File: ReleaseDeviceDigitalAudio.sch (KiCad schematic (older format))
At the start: 7 parts, among them J1 Conn_02x08_Counter_Clockwise

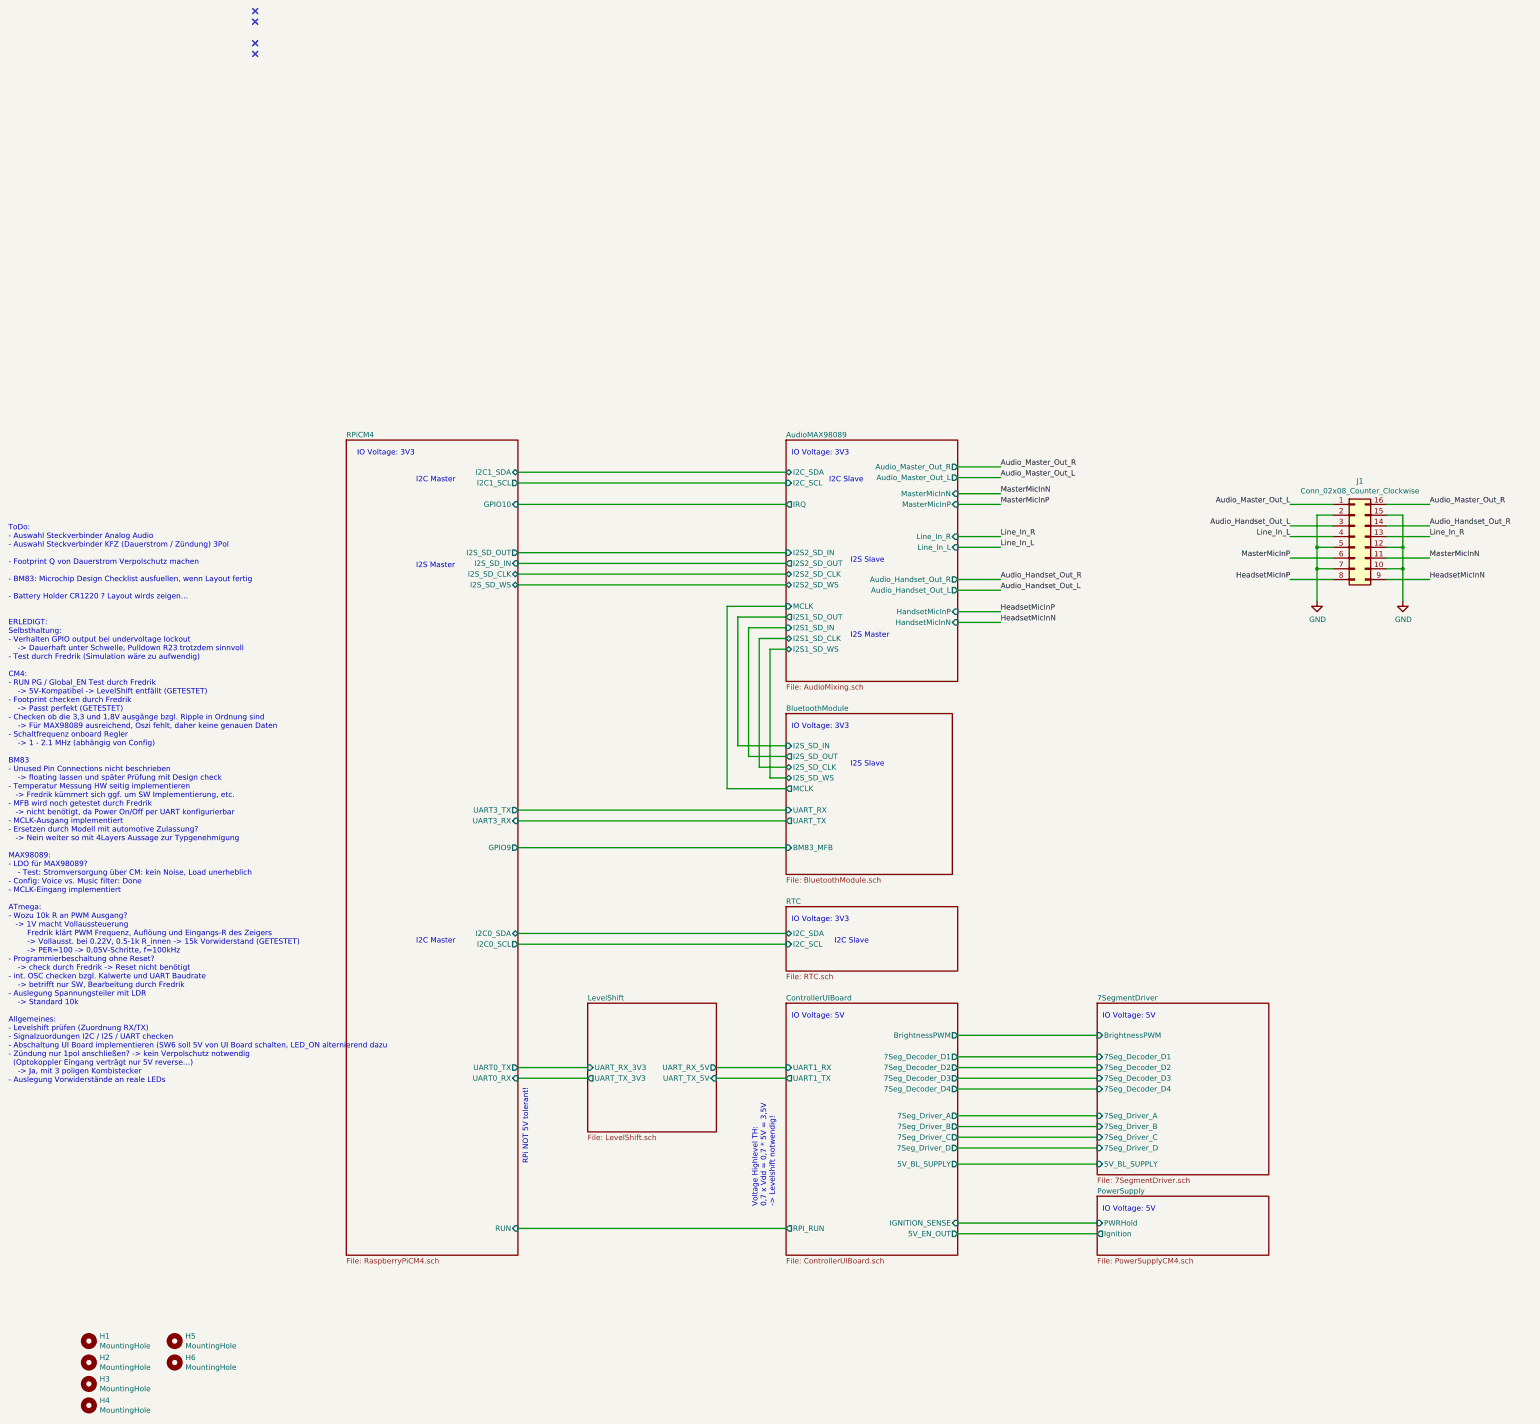
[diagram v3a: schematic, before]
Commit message: - Footprints inkl. 3D model aller Steckverbinder fertig
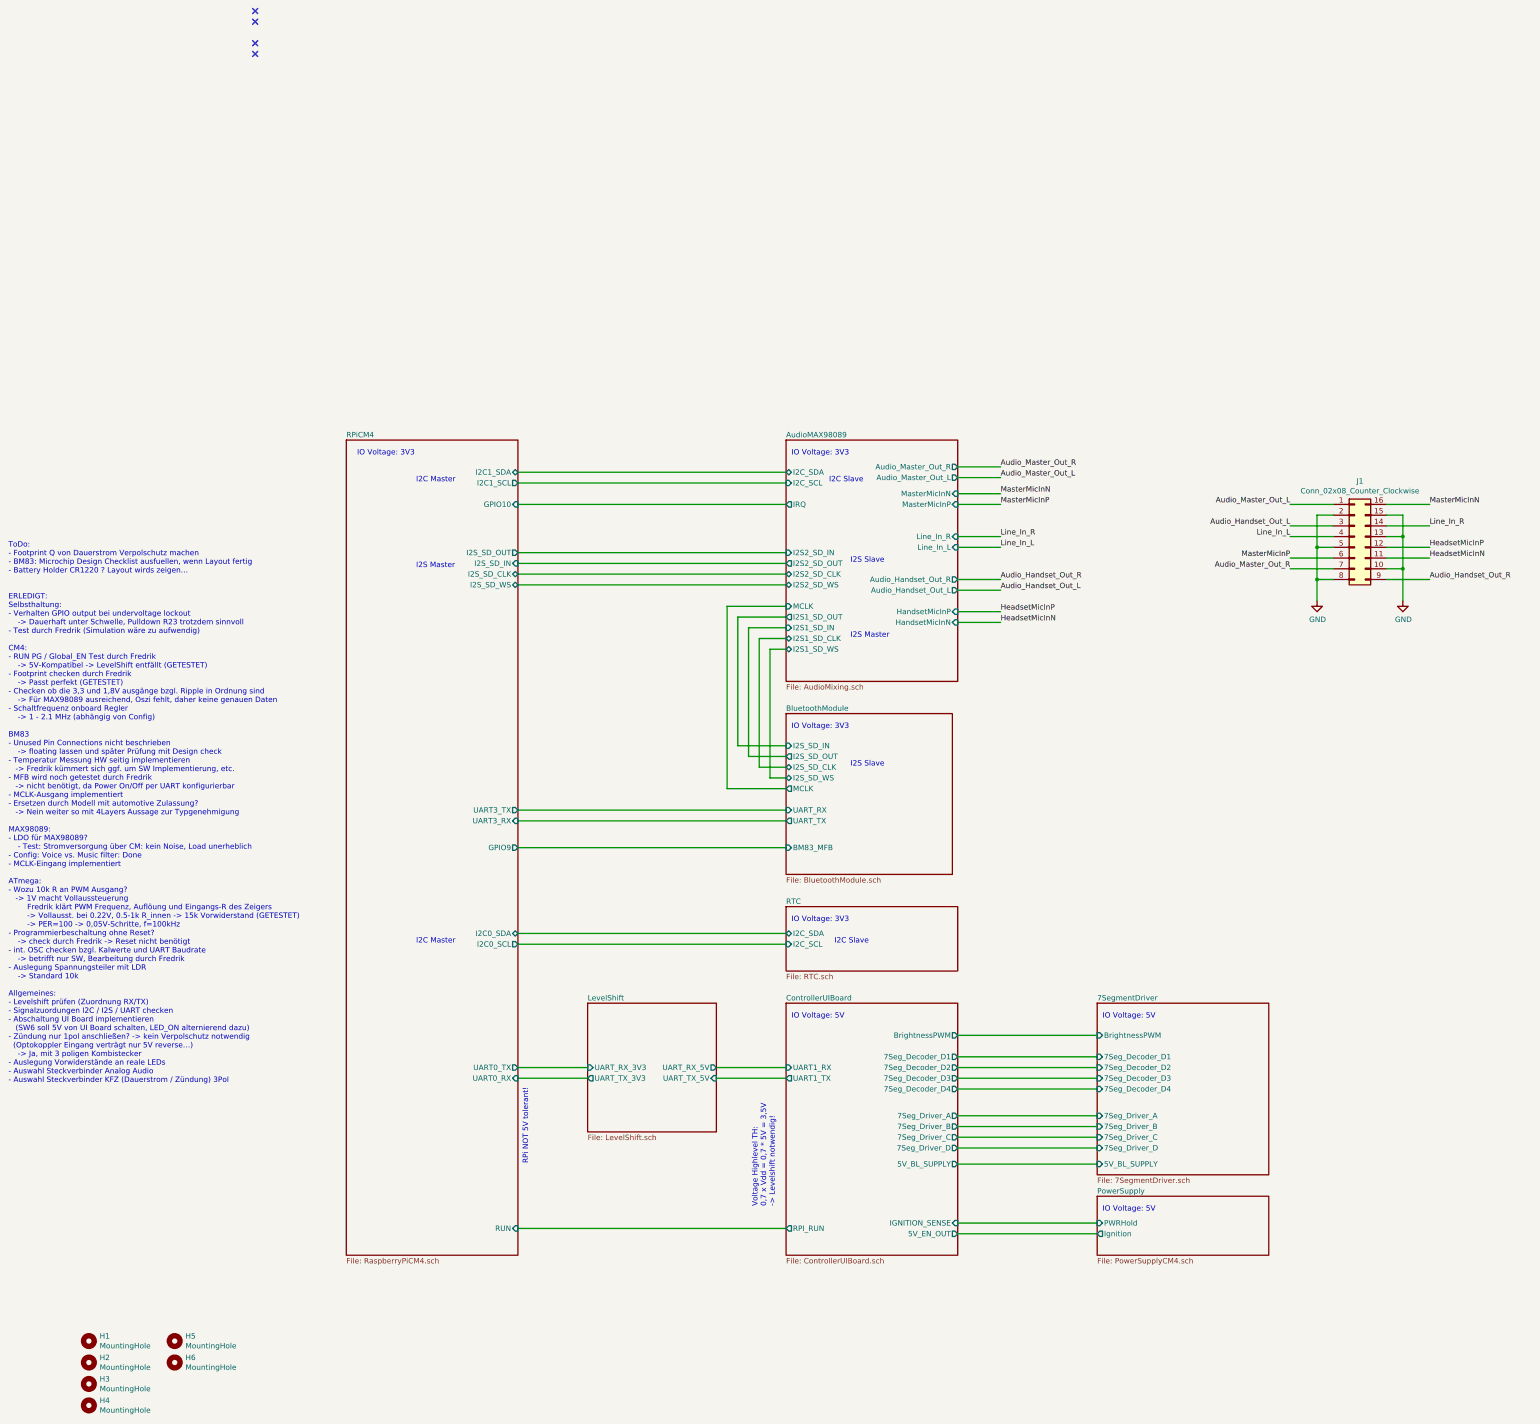
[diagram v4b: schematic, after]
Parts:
- J1: footprint Connector_PinSocket_2.00mm:PinSocket_2x07_P2.00mm_Vertical -> TeKaDe:Molex_34825-0160
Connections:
- net Audio_Handset_Out_R: now also J1.9 (Pin_9); no longer J1.14 (Pin_14)
- net Audio_Master_Out_R: now also J1.7 (Pin_7); no longer J1.16 (Pin_16)
- net GND: now also J1.13 (Pin_13), J1.8 (Pin_8); no longer J1.12 (Pin_12), J1.7 (Pin_7)
- net HeadsetMicInN: now also J1.11 (Pin_11); no longer J1.9 (Pin_9)
- net HeadsetMicInP: now also J1.12 (Pin_12); no longer J1.8 (Pin_8)
- net Line_In_R: now also J1.14 (Pin_14); no longer J1.13 (Pin_13)
- net MasterMicInN: now also J1.16 (Pin_16); no longer J1.11 (Pin_11)
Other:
- note added: "ToDo: \n- Footprint Q von Dauerstrom Verpolschutz machen\n- BM83: Microchip Design Checklist ausfuellen, wenn Layout fertig\n- Battery Holder CR1220 ? Layout wirds zeigen…\n\n\nERLEDIGT:\nSelbsthaltung:\n- Verhalten GPIO output bei undervoltage lockout \n -> Dauerhaft unter Schwelle, Pulldown R23 trotzdem sinnvoll\n- Test durch Fredrik (Simulation wäre zu aufwendig)\n\nCM4: \n- RUN PG / Global_EN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"
- note removed: "ToDo: \n- Auswahl Steckverbinder Analog Audio\n- Auswahl Steckverbinder KFZ (Dauerstrom / Zündung) 3Pol\n\n- Footprint Q von Dauerstrom Verpolschutz machen\n\n- BM83: Microchip Design Checklist ausfuellen, wenn Layout fertig\n\n- Battery Holder CR1220 ? Layout wirds zeigen…\n\n\nERLEDIGT:\nSelbsthaltung:\n- Verhalten GPIO output bei undervoltage lockout \n -> Dauerhaft unter Schwelle, Pulldown R2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"
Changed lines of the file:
@@
 $EndComp
 Text Notes 800  7100 0    50   ~ 0
-ToDo: \n- Auswahl Steckverbinder Analog Audio\n- Auswahl Steckverbinder KFZ (Dauerstrom / Zündung) 3Pol\n\n- Footprint Q von Dauerstrom Verpolschutz machen\n\n- BM83: Microchip Design Checklist ausfuellen, wenn Layout fertig\n\n- Battery Holder CR1220 ? Layout wirds zeigen…\n\n\nERLEDIGT:\nSelbsthaltung:\n- Verhalten GPIO output bei undervoltage lockout \n    -> Dauerhaft unter Schwelle, Pulldown R23 trotzdem sinnvoll\n- Test durch Fredrik (Simulation wäre zu aufwendig)\n\nCM4: \n- RUN PG / Global_EN Test durch Fredrik\n    -> 5V-Kompatibel -> LevelShift entfällt (GETESTET)\n- Footprint checken durch Fredrik\n    -> Passt perfekt (GETESTET)\n- Checken ob die 3,3 und 1,8V ausgänge bzgl. Ripple in Ordnung sind\n    -> Für MAX98089 ausreichend, Oszi fehlt, daher keine genauen Daten\n- Schaltfrequenz onboard Regler\n    -> 1 - 2.1 MHz (abhängig von Config)\n\nBM83\n- Unused Pin Connections nicht beschrieben \n    -> floating lassen und später Prüfung mit Design check\n- Temperatur Messung HW seitig implementieren\n   -> Fredrik kümmert sich ggf. um SW Implementierung, etc.\n- MFB wird noch getestet durch Fredrik  \n   -> nicht benötigt, da Power On/Off per UART konfigurierbar\n- MCLK-Ausgang implementiert\n- Ersetzen durch Modell mit automotive Zulassung?\n   -> Nein weiter so mit 4Layers Aussage zur Typgenehmigung\n\nMAX98089:\n- LDO für MAX98089? \n    - Test: Stromversorgung über CM: kein Noise, Load unerheblich\n- Config: Voice vs. Music filter: Done\n- MCLK-Eingang implementiert\n\nATmega:\n- Wozu 10k R an PWM Ausgang?\n   -> 1V macht Vollaussteuerung\n        Fredrik klärt PWM Frequenz, Auflöung und Eingangs-R des Zeigers\n        -> Vollausst. bei 0.22V, 0.5-1k R_innen -> 15k Vorwiderstand (GETESTET)\n        -> PER=100 -> 0,05V-Schritte, f=100kHz\n- Programmierbeschaltung ohne Reset?\n    -> check durch Fredrik -> Reset nicht benötigt\n- int. OSC checken bzgl. Kalwerte und UART Baudrate\n    -> betrifft nur SW, Bearbeitung durch Fredrik\n- Auslegung Spannungsteiler mit LDR\n    -> Standard 10k\n\nAllgemeines: \n- Levelshift prüfen (Zuordnung RX/TX)\n- Signalzuordungen I2C / I2S / UART checken\n- Abschaltung UI Board implementieren (SW6 soll 5V von UI Board schalten, LED_ON alternierend dazu\n- Zündung nur 1pol anschließen? -> kein Verpolschutz notwendig\n  (Optokoppler Eingang verträgt nur 5V reverse…)\n    -> Ja, mit 3 poligen Kombistecker\n- Auslegung Vorwiderstände an reale LEDs
+ToDo: \n- Footprint Q von Dauerstrom Verpolschutz machen\n- BM83: Microchip Design Checklist ausfuellen, wenn Layout fertig\n- Battery Holder CR1220 ? Layout wirds zeigen…\n\n\nERLEDIGT:\nSelbsthaltung:\n- Verhalten GPIO output bei undervoltage lockout \n    -> Dauerhaft unter Schwelle, Pulldown R23 trotzdem sinnvoll\n- Test durch Fredrik (Simulation wäre zu aufwendig)\n\nCM4: \n- RUN PG / Global_EN Test durch Fredrik\n    -> 5V-Kompatibel -> LevelShift entfällt (GETESTET)\n- Footprint checken durch Fredrik\n    -> Passt perfekt (GETESTET)\n- Checken ob die 3,3 und 1,8V ausgänge bzgl. Ripple in Ordnung sind\n    -> Für MAX98089 ausreichend, Oszi fehlt, daher keine genauen Daten\n- Schaltfrequenz onboard Regler\n    -> 1 - 2.1 MHz (abhängig von Config)\n\nBM83\n- Unused Pin Connections nicht beschrieben \n    -> floating lassen und später Prüfung mit Design check\n- Temperatur Messung HW seitig implementieren\n   -> Fredrik kümmert sich ggf. um SW Implementierung, etc.\n- MFB wird noch getestet durch Fredrik  \n   -> nicht benötigt, da Power On/Off per UART konfigurierbar\n- MCLK-Ausgang implementiert\n- Ersetzen durch Modell mit automotive Zulassung?\n   -> Nein weiter so mit 4Layers Aussage zur Typgenehmigung\n\nMAX98089:\n- LDO für MAX98089? \n    - Test: Stromversorgung über CM: kein Noise, Load unerheblich\n- Config: Voice vs. Music filter: Done\n- MCLK-Eingang implementiert\n\nATmega:\n- Wozu 10k R an PWM Ausgang?\n   -> 1V macht Vollaussteuerung\n        Fredrik klärt PWM Frequenz, Auflöung und Eingangs-R des Zeigers\n        -> Vollausst. bei 0.22V, 0.5-1k R_innen -> 15k Vorwiderstand (GETESTET)\n        -> PER=100 -> 0,05V-Schritte, f=100kHz\n- Programmierbeschaltung ohne Reset?\n    -> check durch Fredrik -> Reset nicht benötigt\n- int. OSC checken bzgl. Kalwerte und UART Baudrate\n    -> betrifft nur SW, Bearbeitung durch Fredrik\n- Auslegung Spannungsteiler mit LDR\n    -> Standard 10k\n\nAllgemeines: \n- Levelshift prüfen (Zuordnung RX/TX)\n- Signalzuordungen I2C / I2S / UART checken\n- Abschaltung UI Board implementieren \n   (SW6 soll 5V von UI Board schalten, LED_ON alternierend dazu)\n- Zündung nur 1pol anschließen? -> kein Verpolschutz notwendig\n  (Optokoppler Eingang verträgt nur 5V reverse…)\n    -> Ja, mit 3 poligen Kombistecker\n- Auslegung Vorwiderstände an reale LEDs\n- Auswahl Steckverbinder Analog Audio\n- Auswahl Steckverbinder KFZ (Dauerstrom / Zündung) 3Pol
 Wire Wire Line
 	9650 2400 10050 2400
@@
 F 0 "J1" H 13400 2517 50  0000 C CNN
 F 1 "Conn_02x08_Counter_Clockwise" H 13400 2426 50  0000 C CNN
-F 2 "Connector_PinSocket_2.00mm:PinSocket_2x07_P2.00mm_Vertical" H 13350 2000 50  0001 C CNN
+F 2 "TeKaDe:Molex_34825-0160" H 13350 2000 50  0001 C CNN
 F 3 "~" H 13350 2000 50  0001 C CNN
 	1    13350 2000
@@
 	13150 2200 12750 2200
 Wire Wire Line
-	13650 2400 14050 2400
-Wire Wire Line
-	13150 2400 12750 2400
+	13650 2200 14050 2200
+Wire Wire Line
+	13650 2100 14050 2100
 Wire Wire Line
 	13150 1900 12750 1900
@@
 	13150 2000 12750 2000
 Wire Wire Line
-	13650 2200 14050 2200
+	13650 1700 14050 1700
 Text Label 12750 1900 2    50   ~ 0
 Audio_Handset_Out_L
-Text Label 14050 1900 0    50   ~ 0
+Text Label 14050 2400 0    50   ~ 0
 Audio_Handset_Out_R
-Text Label 14050 2400 0    50   ~ 0
+Text Label 14050 2200 0    50   ~ 0
 HeadsetMicInN
-Text Label 12750 2400 2    50   ~ 0
+Text Label 14050 2100 0    50   ~ 0
 HeadsetMicInP
 Text Label 12750 1700 2    50   ~ 0
 Audio_Master_Out_L
+Text Label 12750 2300 2    50   ~ 0
+Audio_Master_Out_R
 Text Label 14050 1700 0    50   ~ 0
-Audio_Master_Out_R
-Text Label 14050 2200 0    50   ~ 0
 MasterMicInN
 Text Label 12750 2200 2    50   ~ 0
 MasterMicInP
-Text Label 14050 2000 0    50   ~ 0
+Text Label 14050 1900 0    50   ~ 0
 Line_In_R
 Text Label 12750 2000 2    50   ~ 0
 Line_In_L
 Wire Wire Line
-	13650 2000 14050 2000
-Wire Wire Line
-	13650 1700 14050 1700
-Wire Wire Line
 	13650 1900 14050 1900
+Wire Wire Line
+	13150 2300 12750 2300
+Wire Wire Line
+	13650 2400 14050 2400
 Wire Wire Line
 	13000 1800 13000 2100
@@
 Connection ~ 13000 2100
 Wire Wire Line
-	13150 2300 13000 2300
-Wire Wire Line
-	13000 2100 13000 2300
-Connection ~ 13000 2300
-Wire Wire Line
-	13000 2300 13000 2600
+	13150 2400 13000 2400
 $Comp
 L power:GND #PWR0183
@@
 	13650 1800 13800 1800
 Wire Wire Line
-	13800 1800 13800 2100
-Wire Wire Line
-	13650 2100 13800 2100
-Connection ~ 13800 2100
-Wire Wire Line
-	13800 2100 13800 2300
+	13800 1800 13800 2000
+Wire Wire Line
+	13650 2000 13800 2000
 Wire Wire Line
 	13650 2300 13800 2300
@@
 Wire Wire Line
 	13800 2300 13800 2600
+Connection ~ 13000 2400
+Wire Wire Line
+	13000 2400 13000 2600
+Wire Wire Line
+	13000 2100 13000 2400
+Connection ~ 13800 2000
+Wire Wire Line
+	13800 2000 13800 2300
 $EndSCHEMATC
